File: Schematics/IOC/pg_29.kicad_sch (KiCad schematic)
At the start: 18 parts, among them U2901 F374, U2902 F374, U2903 F374, U2904 F374, U2905 F280, U2906 F280, U2907 F280, U2908 F280, U2909 F374, U2910 F20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

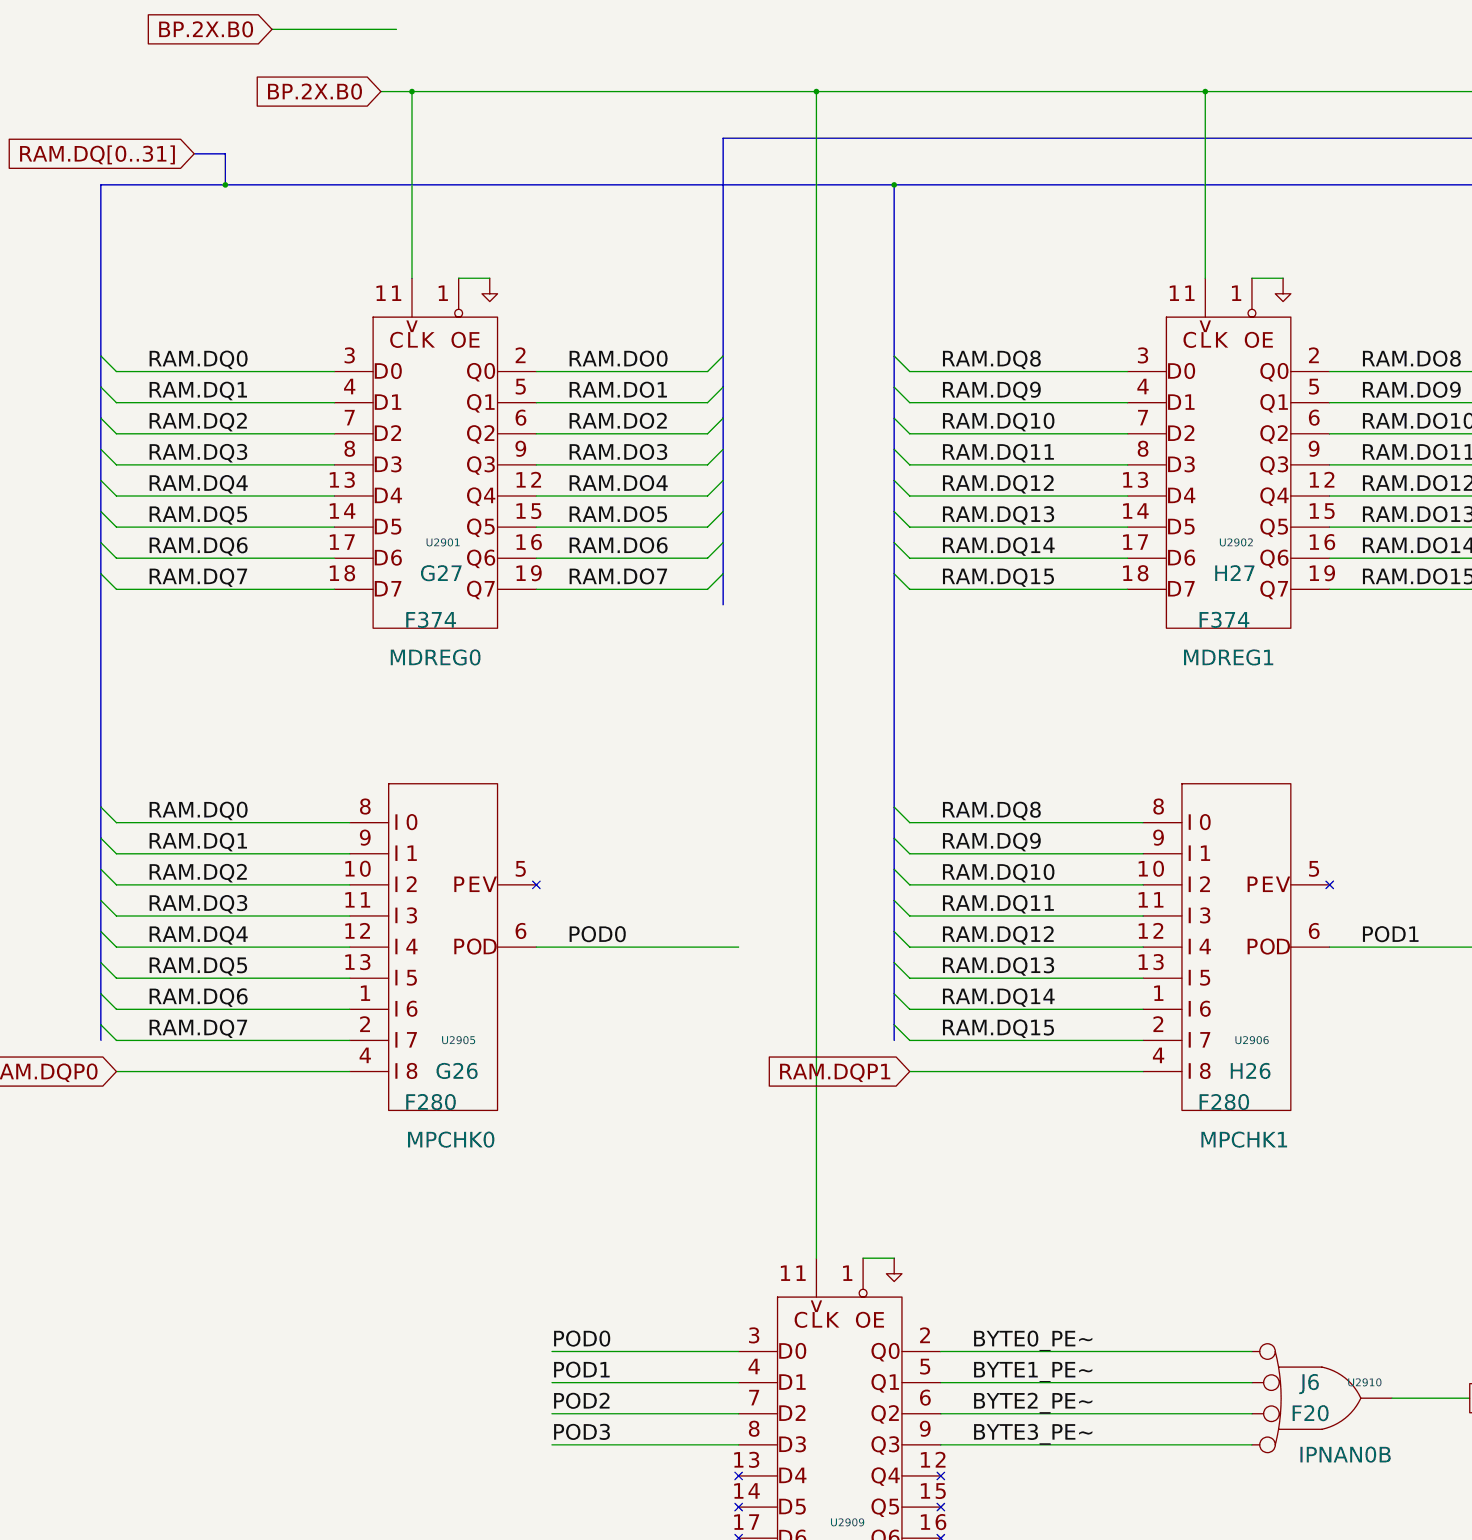
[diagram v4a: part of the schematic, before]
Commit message: Implement IOC RAM as single mega-component
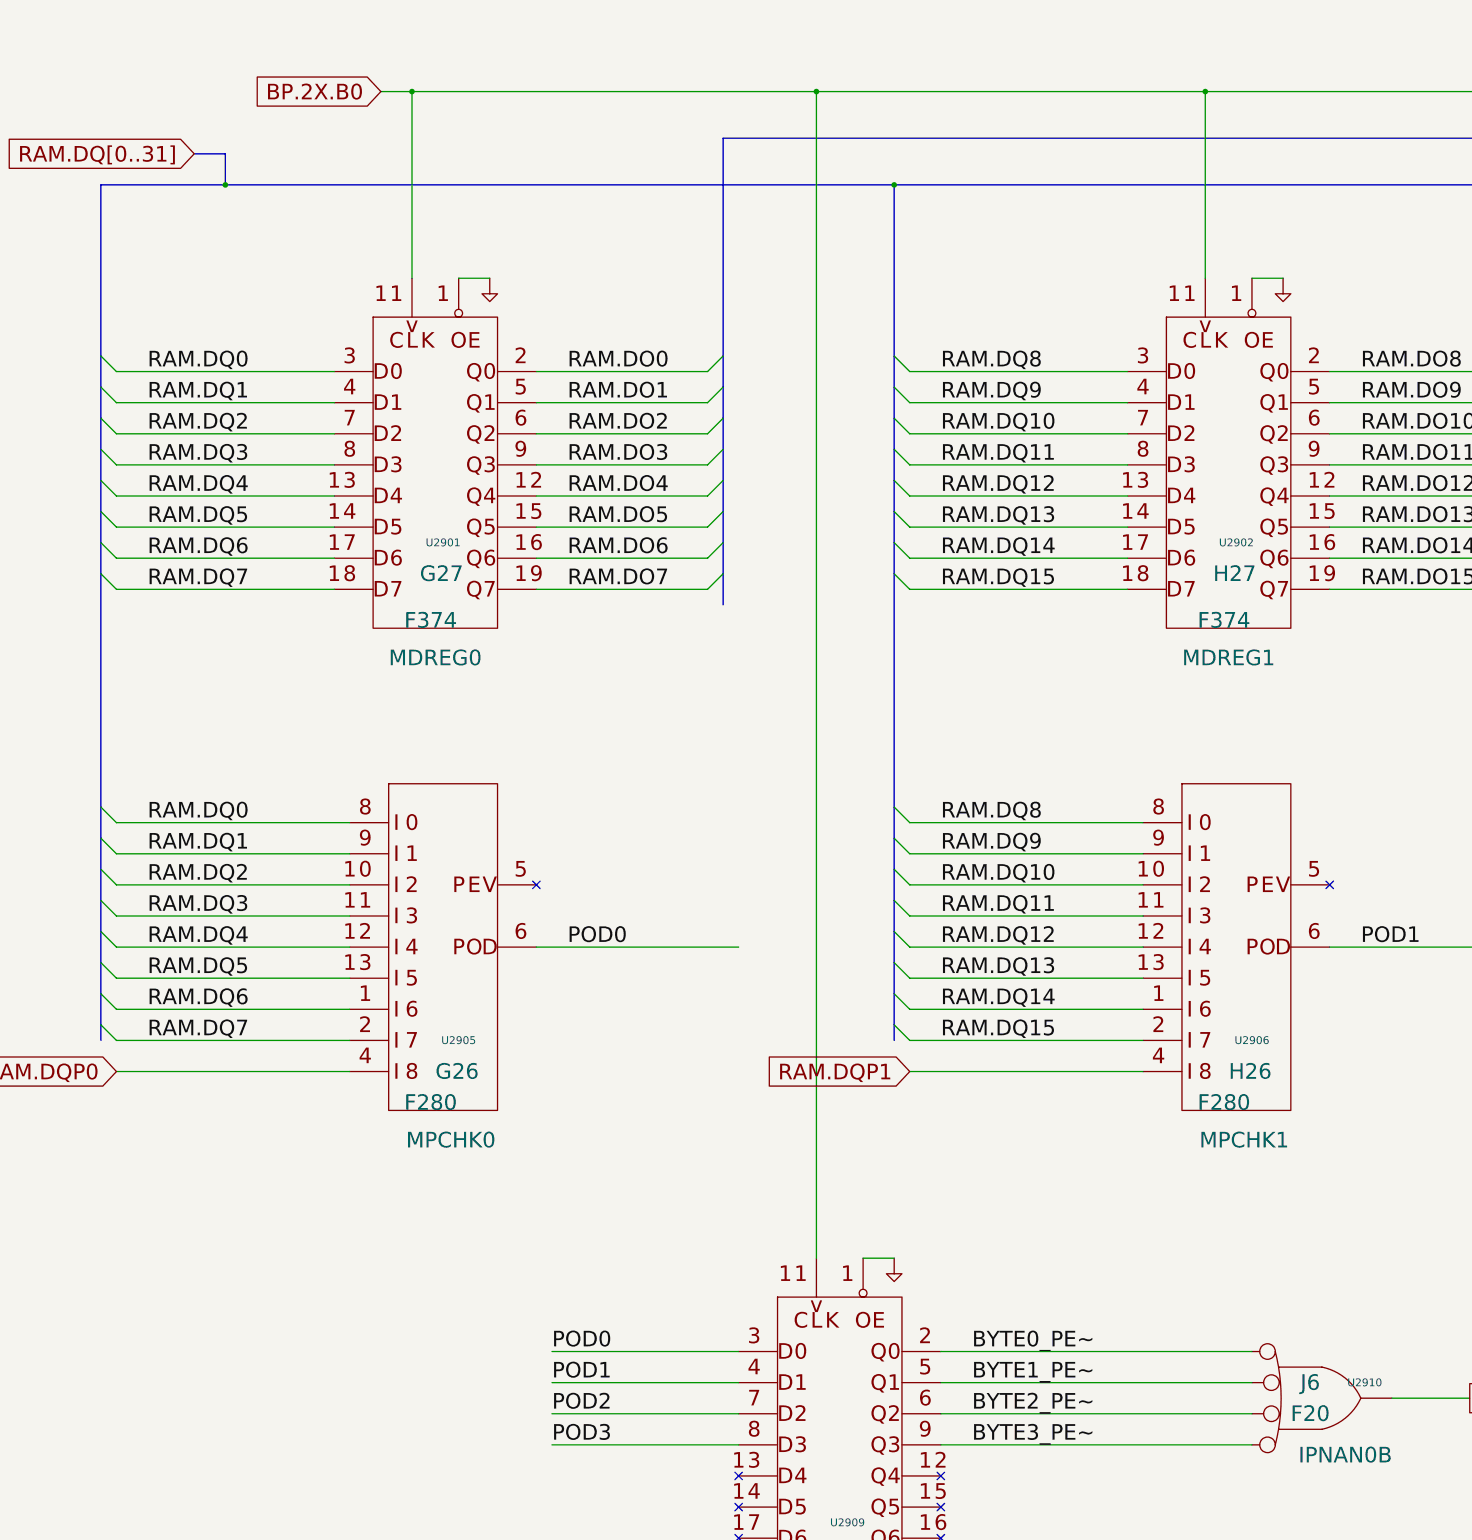
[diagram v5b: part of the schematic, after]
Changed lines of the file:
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@@
-  (wire
-    (pts
-      (xy 63.5 12.7)
-      (xy 83.82 12.7)
-    )
-    (stroke
-      (width 0)
-      (type default)
-      (color 0 0 0 0)
-    )
-  )
   (wire
     (pts
@@
       (effects
         (font
-          (size 2.54 2.54)
-        )
-        (justify right)
-      )
-    )
-  )
-  (global_label
-    "BP.2X.B0"
-    (shape input)
-    (at 63.5 12.7 180)
-    (fields_autoplaced)
-    (effects
-      (font
-        (size 2.54 2.54)
-      )
-      (justify right)
-    )
-    (property
-      "Intersheet References"
-      "${INTERSHEET_REFS}"
-      (id 0)
-      (at 38.9406 12.5413 0)
-      (effects
-        (font
